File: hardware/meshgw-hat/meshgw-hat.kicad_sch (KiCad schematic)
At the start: 5 parts, among them J1 RPi 40-pin GPIO, U1 E22-900M30S

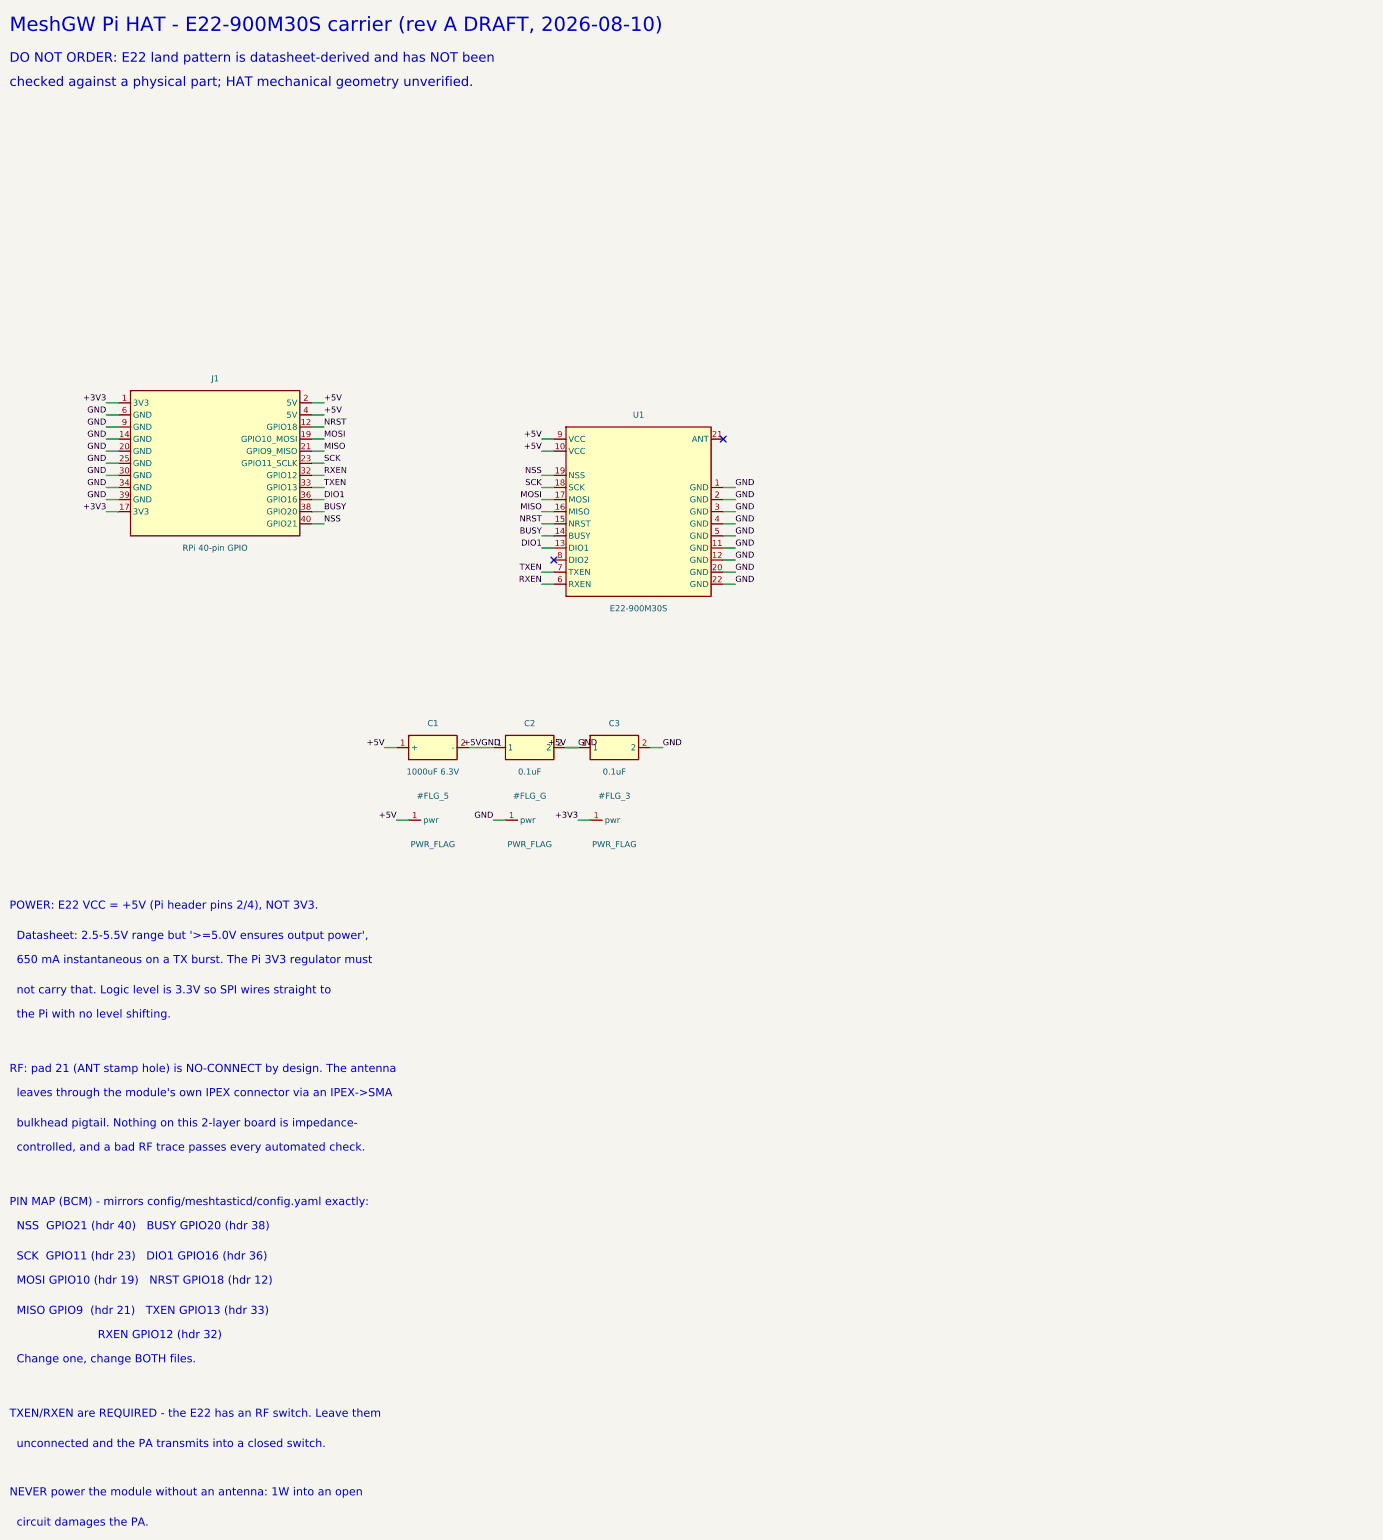
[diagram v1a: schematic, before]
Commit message: meshgw HAT: verify mechanical geometry vs Pi 3B+, unify netlist, fix schematic short
The HAT geometry was unverified against the official Raspberry Pi HAT spec,
as route.sh itself warned. Verified against three independent sources (the
HAT mechanical PDF, the Pi 3B+ drawing, and KiCad's own HAT template plus its
Pi Zero socketed footprint). It was wrong six ways while passing DRC with
0 violations and 0 unconnected:

  - header rows swapped: every SPI signal onto its neighbour's pin
  - header origin (7.0, 2.5) instead of (8.37, 4.77): would not seat at all
  - 56.5 mm tall: that is the SMT-header figure, through-hole needs 56.0
  - square corners against a spec mandating R3
  - pour flooded to 0.5 mm of mounting holes needing a 6.2 mm isolated land
  - no clearance for the Pi 3B+ PoE header J14

J14 gets an edge-open notch rather than an enclosed cutout: it leaves ~1 mm
to the board edge, and it can carry ~48-57 V on a PoE switch.

New check_geometry.py asserts 27 of these facts against the ROUTED board and
route.sh runs it, because a clean DRC is not a negative control for geometry.

New netlist.py is the single pinout source. gen.py and gen_pcb.py each held a
copy 'mirroring' each other and had silently stopped; config/meshtasticd/
config.yaml had the old map too. GPIO map re-pinned off the MeshAdv-Pi-Hat
reference onto odd (inner-row) header pins -- forced, because four nets could
not be routed otherwise, and kept because GPIO5 idles chip-select deselected
where GPIO21 asserted it on every boot.

Separately, the SCHEMATIC had no GND net at all: C1/C2/C3 sat 5.08 mm apart
in a row, place() draws a 2.54 mm stub per pin, so adjacent stubs met and
shorted GND to +5V into a 27-node '+5V'. Invisible to every board-side check
because gen_pcb.py never reads the sheet. Caps stacked vertically, and
check_netlist.py now asserts the exported schematic netlist equals netlist.py.

Board: 119 segments, 0 vias, DRC 0/0, ERC 0, 27/27 mechanical checks.
Still DRAFT - DO NOT ORDER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
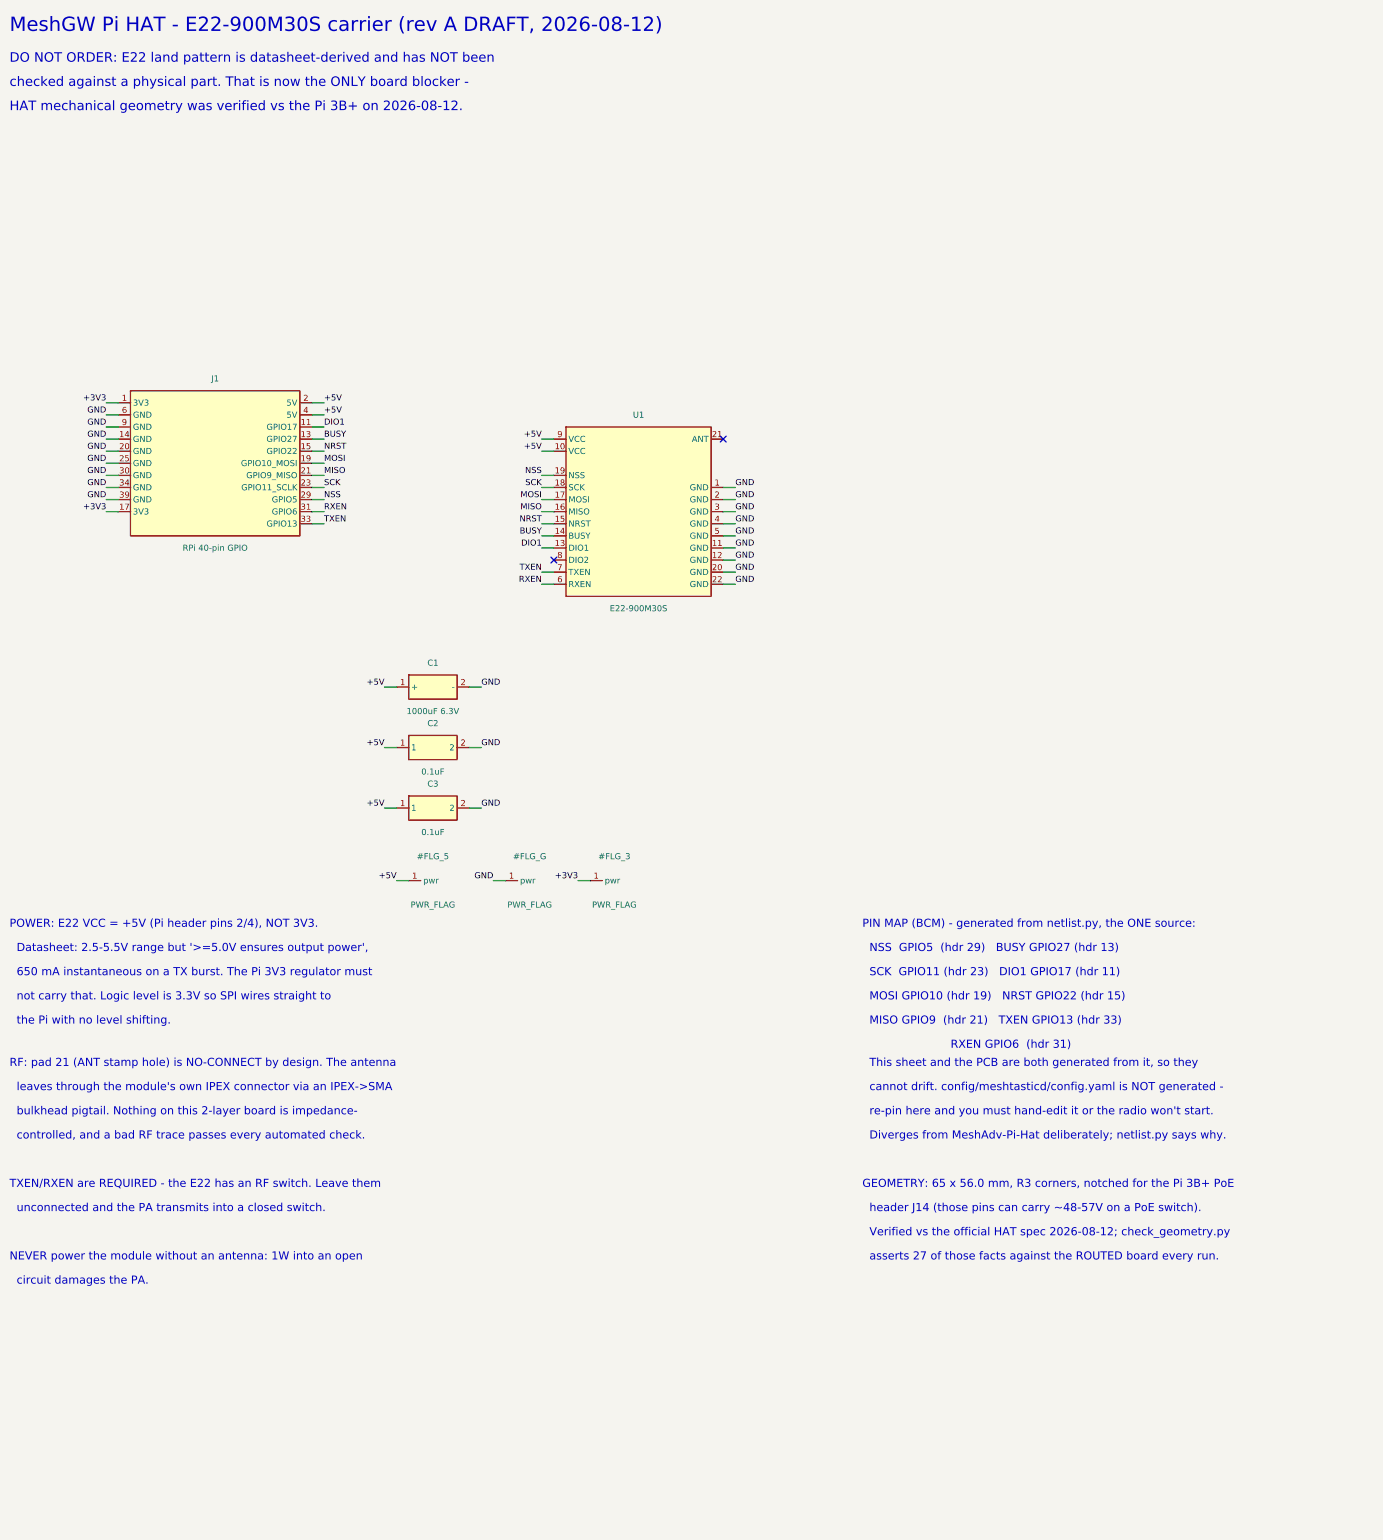
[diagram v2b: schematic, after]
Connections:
- net +5V: no longer C1.2 (-), C2.2, C3.2, J1.14 (GND), J1.20 (GND), J1.25 (GND), J1.30 (GND), J1.34 (GND), J1.39 (GND), J1.6 (GND), J1.9 (GND), U1.1 (GND), U1.11 (GND), U1.12 (GND), U1.2 (GND), U1.20 (GND), U1.22 (GND), U1.3 (GND), U1.4 (GND), U1.5 (GND)
- net BUSY: now also J1.13 (GPIO27); no longer J1.38 (GPIO20)
- net DIO1: now also J1.11 (GPIO17); no longer J1.36 (GPIO16)
- net NRST: now also J1.15 (GPIO22); no longer J1.12 (GPIO18)
- net NSS: now also J1.29 (GPIO5); no longer J1.40 (GPIO21)
- net RXEN: now also J1.31 (GPIO6); no longer J1.32 (GPIO12)
- new net GND: C1.2 (-), C2.2, C3.2, J1.14 (GND), J1.20 (GND), J1.25 (GND), J1.30 (GND), J1.34 (GND), J1.39 (GND), J1.6 (GND), J1.9 (GND), U1.1 (GND), U1.11 (GND), U1.12 (GND), U1.2 (GND), U1.20 (GND), U1.22 (GND), U1.3 (GND), U1.4 (GND), U1.5 (GND)
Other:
- note added: "Diverges from MeshAdv-Pi-Hat deliberately; netlist.py says why."
- note added: "GEOMETRY: 65 x 56.0 mm, R3 corners, notched for the Pi 3B+ PoE"
- note added: "HAT mechanical geometry was verified vs the Pi 3B+ on 2026-08-12."
- note added: "MOSI GPIO10 (hdr 19) NRST GPIO22 (hdr 15)"
- note added: "MeshGW Pi HAT - E22-900M30S carrier (rev A DRAFT, 2026-08-12)"
- note added: "NSS GPIO5 (hdr 29) BUSY GPIO27 (hdr 13)"
- note added: "PIN MAP (BCM) - generated from netlist.py, the ONE source:"
- note added: "RXEN GPIO6 (hdr 31)"
- note added: "SCK GPIO11 (hdr 23) DIO1 GPIO17 (hdr 11)"
- note added: "This sheet and the PCB are both generated from it, so they"
- note added: "Verified vs the official HAT spec 2026-08-12; check_geometry.py"
- note added: "asserts 27 of those facts against the ROUTED board every run."
- note added: "cannot drift. config/meshtasticd/config.yaml is NOT generated -"
- note added: "checked against a physical part. That is now the ONLY board blocker -"
- note added: "header J14 (those pins can carry ~48-57V on a PoE switch)."
- note added: "re-pin here and you must hand-edit it or the radio won't start."
- note removed: "Change one, change BOTH files."
- note removed: "MOSI GPIO10 (hdr 19) NRST GPIO18 (hdr 12)"
- note removed: "MeshGW Pi HAT - E22-900M30S carrier (rev A DRAFT, 2026-08-10)"
- note removed: "NSS GPIO21 (hdr 40) BUSY GPIO20 (hdr 38)"
- note removed: "PIN MAP (BCM) - mirrors config/meshtasticd/config.yaml exactly:"
- note removed: "RXEN GPIO12 (hdr 32)"
- note removed: "SCK GPIO11 (hdr 23) DIO1 GPIO16 (hdr 36)"
- note removed: "checked against a physical part; HAT mechanical geometry unverified."

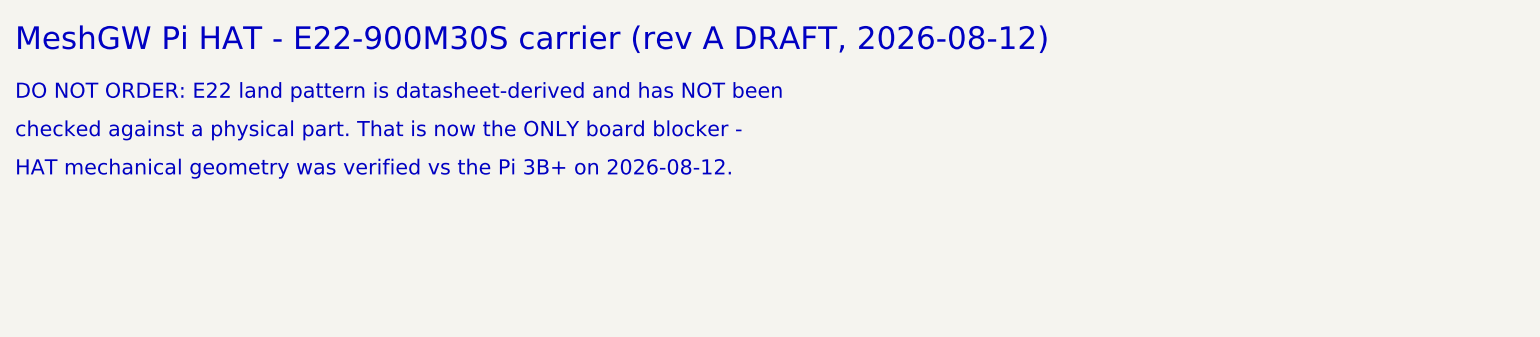
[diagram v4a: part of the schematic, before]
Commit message: meshgw HAT: clear rev A to order, build the fab package
Don's call 2026-08-12: batch the bare board into the shared JLCPCB checkout
with OSL, FD2, pool and Sentinel. Boards are ~$2 against $6-25 shipping, so
holding it back would pay that shipping charge again later with certainty.

U1's land pattern has still never met a physical module -- the E22 was ordered
the same day and is weeks out. fab_gate.py therefore keeps GEOMETRY_VERIFIED
False and carries a SEPARATE GEOMETRY_OVERRIDE string naming who decided, when
and why. Flipping the flag would have been one character and would have
destroyed the distinction between 'we checked' and 'we accepted the risk',
which is exactly what a reader six weeks from now needs.

The risk is real: the E22 solders to castellated pads, so a wrong land pattern
makes these boards scrap -- unlike Sentinel, whose open items were modules on
headers where a wrong guess costs a module, not a respin.

Silk changed from 'DO NOT ORDER - E22 land pattern unverified', which would be
false on a board ordered on purpose, to 'U1 LAND UNVERIFIED - CHECK FIT BEFORE
SOLDERING' -- a warning aimed at the moment it can still act. Checking a land
pattern is free before the iron and impossible after.

make_fab.sh follows Sentinel's, carrying its traps (PROTEL extensions not .gbr,
--excellon-units not --units, report-file DRC phrasing, board-file-derived
prefix) and adding a drill-size assert against JLCPCB's 0.30 mm minimum, which
nothing else in the chain checks. Smallest hole here is 0.80 mm.

Package: 12 members, every layer asserted by name, DRC and 27 mechanical
checks re-run on the fab copy rather than inherited.

Co-Authored-By: Claude Opus 5 <noreply@anthropic.com>
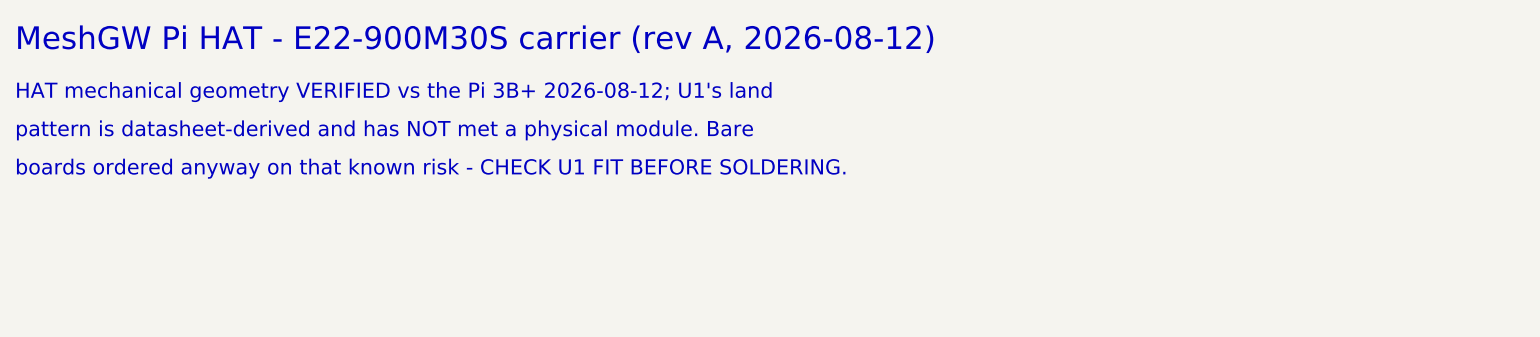
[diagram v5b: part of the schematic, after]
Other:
- note added: "HAT mechanical geometry VERIFIED vs the Pi 3B+ 2026-08-12; U1's land"
- note added: "MeshGW Pi HAT - E22-900M30S carrier (rev A, 2026-08-12)"
- note added: "boards ordered anyway on that known risk - CHECK U1 FIT BEFORE SOLDERING."
- note added: "pattern is datasheet-derived and has NOT met a physical module. Bare"
- note removed: "DO NOT ORDER: E22 land pattern is datasheet-derived and has NOT been"
- note removed: "HAT mechanical geometry was verified vs the Pi 3B+ on 2026-08-12."
- note removed: "MeshGW Pi HAT - E22-900M30S carrier (rev A DRAFT, 2026-08-12)"
- note removed: "checked against a physical part. That is now the ONLY board blocker -"
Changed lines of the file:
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@@
     (pin "33")
     (instances (project "meshgw-hat"
-      (path "/33349a9d-9a2b-4764-be09-58eddc9c7f26" (reference "J1") (unit 1))))
+      (path "/80503a93-a82c-47f8-990a-89053b6683b0" (reference "J1") (unit 1))))
   )
   (wire (pts (xy 43.18 95.25) (xy 40.64 95.25)) (stroke (width 0) (type default)))
@@
     (pin "22")
     (instances (project "meshgw-hat"
-      (path "/33349a9d-9a2b-4764-be09-58eddc9c7f26" (reference "U1") (unit 1))))
+      (path "/80503a93-a82c-47f8-990a-89053b6683b0" (reference "U1") (unit 1))))
   )
   (wire (pts (xy 170.18 110.49) (xy 172.72 110.49)) (stroke (width 0) (type default)))
@@
     (pin "2")
     (instances (project "meshgw-hat"
-      (path "/33349a9d-9a2b-4764-be09-58eddc9c7f26" (reference "C1") (unit 1))))
+      (path "/80503a93-a82c-47f8-990a-89053b6683b0" (reference "C1") (unit 1))))
   )
   (wire (pts (xy 101.6 152.4) (xy 99.06 152.4)) (stroke (width 0) (type default)))
@@
     (pin "2")
     (instances (project "meshgw-hat"
-      (path "/33349a9d-9a2b-4764-be09-58eddc9c7f26" (reference "C2") (unit 1))))
+      (path "/80503a93-a82c-47f8-990a-89053b6683b0" (reference "C2") (unit 1))))
   )
   (wire (pts (xy 101.6 165.1) (xy 99.06 165.1)) (stroke (width 0) (type default)))
@@
     (pin "2")
     (instances (project "meshgw-hat"
-      (path "/33349a9d-9a2b-4764-be09-58eddc9c7f26" (reference "C3") (unit 1))))
+      (path "/80503a93-a82c-47f8-990a-89053b6683b0" (reference "C3") (unit 1))))
   )
   (wire (pts (xy 101.6 177.8) (xy 99.06 177.8)) (stroke (width 0) (type default)))
@@
     (pin "1")
     (instances (project "meshgw-hat"
-      (path "/33349a9d-9a2b-4764-be09-58eddc9c7f26" (reference "#FLG_5") (unit 1))))
+      (path "/80503a93-a82c-47f8-990a-89053b6683b0" (reference "#FLG_5") (unit 1))))
   )
   (wire (pts (xy 104.14 193.04) (xy 101.6 193.04)) (stroke (width 0) (type default)))
@@
     (pin "1")
     (instances (project "meshgw-hat"
-      (path "/33349a9d-9a2b-4764-be09-58eddc9c7f26" (reference "#FLG_G") (unit 1))))
+      (path "/80503a93-a82c-47f8-990a-89053b6683b0" (reference "#FLG_G") (unit 1))))
   )
   (wire (pts (xy 124.46 193.04) (xy 121.92 193.04)) (stroke (width 0) (type default)))
@@
     (pin "1")
     (instances (project "meshgw-hat"
-      (path "/33349a9d-9a2b-4764-be09-58eddc9c7f26" (reference "#FLG_3") (unit 1))))
+      (path "/80503a93-a82c-47f8-990a-89053b6683b0" (reference "#FLG_3") (unit 1))))
   )
   (wire (pts (xy 142.24 193.04) (xy 139.7 193.04)) (stroke (width 0) (type default)))
   (label "+3V3" (at 139.7 193.04 180)
     (effects (font (size 1.27 1.27)) (justify right bottom)))
-  (text "MeshGW Pi HAT - E22-900M30S carrier (rev A DRAFT, 2026-08-12)" (at 20.32 15.24 0) (effects (font (size 3.0 3.0)) (justify left bottom)))
-  (text "DO NOT ORDER: E22 land pattern is datasheet-derived and has NOT been" (at 20.32 21.59 0) (effects (font (size 2.0 2.0)) (justify left bottom)))
-  (text "checked against a physical part. That is now the ONLY board blocker -" (at 20.32 26.67 0) (effects (font (size 2.0 2.0)) (justify left bottom)))
-  (text "HAT mechanical geometry was verified vs the Pi 3B+ on 2026-08-12." (at 20.32 31.75 0) (effects (font (size 2.0 2.0)) (justify left bottom)))
+  (text "MeshGW Pi HAT - E22-900M30S carrier (rev A, 2026-08-12)" (at 20.32 15.24 0) (effects (font (size 3.0 3.0)) (justify left bottom)))
+  (text "HAT mechanical geometry VERIFIED vs the Pi 3B+ 2026-08-12; U1's land" (at 20.32 21.59 0) (effects (font (size 2.0 2.0)) (justify left bottom)))
+  (text "pattern is datasheet-derived and has NOT met a physical module. Bare" (at 20.32 26.67 0) (effects (font (size 2.0 2.0)) (justify left bottom)))
+  (text "boards ordered anyway on that known risk - CHECK U1 FIT BEFORE SOLDERING." (at 20.32 31.75 0) (effects (font (size 2.0 2.0)) (justify left bottom)))
   (text "POWER: E22 VCC = +5V (Pi header pins 2/4), NOT 3V3." (at 20.32 203.2 0) (effects (font (size 1.7 1.7)) (justify left bottom)))
   (text "  Datasheet: 2.5-5.5V range but '>=5.0V ensures output power'," (at 20.32 208.28 0) (effects (font (size 1.7 1.7)) (justify left bottom)))
